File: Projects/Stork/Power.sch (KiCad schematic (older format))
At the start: 14 parts, among them J25 Conn_02x03_Odd_Even, J26 Conn_01x03_Male, J27 Screw_Terminal_01x02, J28 Conn_01x03_Male, J29 Conn_01x03_Male, J30 Conn_01x03_Male, U50 TPS79330-EP, U51 TPS73150DBV

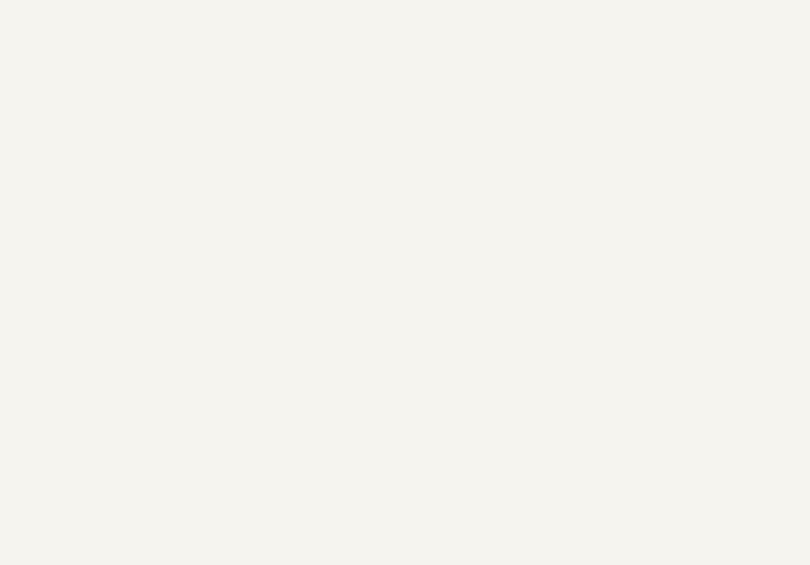
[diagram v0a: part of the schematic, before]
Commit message: added mounting hole in schematic and corresponding footprint on layout
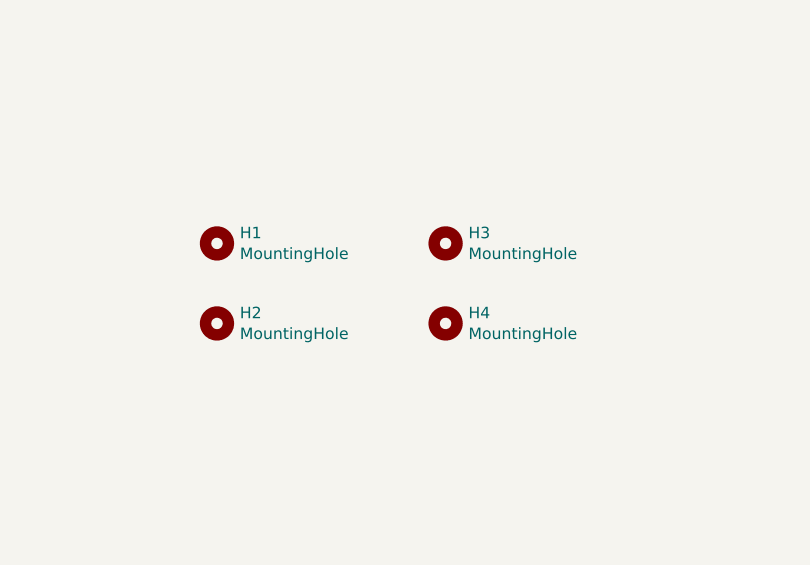
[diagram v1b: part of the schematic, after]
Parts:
- added H1, H2, H3, H4: MountingHole, MountingHole:MountingHole_2.5mm_Pad, symbol Mechanical:MountingHole
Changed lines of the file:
@@
 Wire Wire Line
 	2650 4350 3400 4350
+$Comp
+L Mechanical:MountingHole H1
+U 1 1 5E743F5A
+P 6500 3850
+F 0 "H1" H 6600 3896 50  0000 L CNN
+F 1 "MountingHole" H 6600 3805 50  0000 L CNN
+F 2 "MountingHole:MountingHole_2.5mm_Pad" H 6500 3850 50  0001 C CNN
+F 3 "~" H 6500 3850 50  0001 C CNN
+	1    6500 3850
+	1    0    0    -1
+$EndComp
+$Comp
+L Mechanical:MountingHole H3
+U 1 1 5E74AFC2
+P 7500 3850
+F 0 "H3" H 7600 3896 50  0000 L CNN
+F 1 "MountingHole" H 7600 3805 50  0000 L CNN
+F 2 "MountingHole:MountingHole_2.5mm_Pad" H 7500 3850 50  0001 C CNN
+F 3 "~" H 7500 3850 50  0001 C CNN
+	1    7500 3850
+	1    0    0    -1
+$EndComp
+$Comp
+L Mechanical:MountingHole H2
+U 1 1 5E74C1EE
+P 6500 4200
+F 0 "H2" H 6600 4246 50  0000 L CNN
+F 1 "MountingHole" H 6600 4155 50  0000 L CNN
+F 2 "MountingHole:MountingHole_2.5mm_Pad" H 6500 4200 50  0001 C CNN
+F 3 "~" H 6500 4200 50  0001 C CNN
+	1    6500 4200
+	1    0    0    -1
+$EndComp
+$Comp
+L Mechanical:MountingHole H4
+U 1 1 5E74D363
+P 7500 4200
+F 0 "H4" H 7600 4246 50  0000 L CNN
+F 1 "MountingHole" H 7600 4155 50  0000 L CNN
+F 2 "MountingHole:MountingHole_2.5mm_Pad" H 7500 4200 50  0001 C CNN
+F 3 "~" H 7500 4200 50  0001 C CNN
+	1    7500 4200
+	1    0    0    -1
+$EndComp
 $EndSCHEMATC

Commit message: changed power pin to dc barrel jack
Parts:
- removed J27: Screw_Terminal_01x02, Connector_Molex:Molex_KK-254_AE-6410-02A_1x02_P2.54mm_Vertical, symbol Connector:Screw_Terminal_01x02
- added J?: Barrel_Jack_Switch, footprint:FC681465P, symbol Connector:Barrel_Jack_Switch
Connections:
- wire segments 58 -> 59
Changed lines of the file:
@@
 	1    0    0    -1
 $EndComp
-$Comp
-L Connector:Screw_Terminal_01x02 J27
-U 1 1 5E4E8DF0
-P 1450 2200
-F 0 "J27" H 1530 2192 50  0000 L CNN
-F 1 "Screw_Terminal_01x02" H 1530 2101 50  0000 L CNN
-F 2 "Connector_Molex:Molex_KK-254_AE-6410-02A_1x02_P2.54mm_Vertical" H 1450 2200 50  0001 C CNN
-F 3 "~" H 1450 2200 50  0001 C CNN
-	1    1450 2200
-	-1   0    0    1
-$EndComp
-$Comp
-L power:GND #PWR0152
-U 1 1 5E4ECFCC
-P 2050 2250
-F 0 "#PWR0152" H 2050 2000 50  0001 C CNN
-F 1 "GND" H 2055 2077 50  0000 C CNN
-F 2 "" H 2050 2250 50  0001 C CNN
-F 3 "" H 2050 2250 50  0001 C CNN
-	1    2050 2250
-	1    0    0    -1
-$EndComp
-Wire Wire Line
-	2050 2200 2050 2250
 Text GLabel 5450 1100 2    50   Input ~ 0
 5V_CoraZ7
@@
 Wire Wire Line
 	5300 2400 5150 2400
-Text GLabel 1950 2100 2    50   Input ~ 0
-V_RAW
-Wire Wire Line
-	1600 2100 1650 2100
-Wire Wire Line
-	1650 2100 1950 2100
-Connection ~ 1650 2100
-Wire Wire Line
-	1650 2200 2050 2200
 Wire Wire Line
 	5150 1100 5450 1100
@@
 	1    0    0    -1
 $EndComp
+$Comp
+L Connector:Barrel_Jack_Switch J?
+U 1 1 5EA23779
+P 1050 2200
+F 0 "J?" H 1107 2517 50  0000 C CNN
+F 1 "Barrel_Jack_Switch" H 1107 2426 50  0000 C CNN
+F 2 "footprint:FC681465P" H 1100 2160 50  0001 C CNN
+F 3 "~" H 1100 2160 50  0001 C CNN
+	1    1050 2200
+	1    0    0    -1
+$EndComp
+$Comp
+L power:GND #PWR?
+U 1 1 5EA2418A
+P 1550 2350
+F 0 "#PWR?" H 1550 2100 50  0001 C CNN
+F 1 "GND" H 1555 2177 50  0000 C CNN
+F 2 "" H 1550 2350 50  0001 C CNN
+F 3 "" H 1550 2350 50  0001 C CNN
+	1    1550 2350
+	1    0    0    -1
+$EndComp
+Wire Wire Line
+	1350 2300 1550 2300
+Wire Wire Line
+	1550 2300 1550 2350
+Wire Wire Line
+	1350 2200 1550 2200
+Wire Wire Line
+	1550 2200 1550 2300
+Connection ~ 1550 2300
+Text GLabel 1450 2100 2    50   Input ~ 0
+V_RAW
+Wire Wire Line
+	1350 2100 1450 2100
 $EndSCHEMATC

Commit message: added logo
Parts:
- gave numbers to parts that had none: 1
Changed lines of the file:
@@
 $EndComp
 $Comp
-L Connector:Barrel_Jack_Switch J?
+L Connector:Barrel_Jack_Switch J1
 U 1 1 5EA23779
 P 1050 2200
-F 0 "J?" H 1107 2517 50  0000 C CNN
+F 0 "J1" H 1107 2517 50  0000 C CNN
 F 1 "Barrel_Jack_Switch" H 1107 2426 50  0000 C CNN
 F 2 "footprint:FC681465P" H 1100 2160 50  0001 C CNN
@@
 $EndComp
 $Comp
-L power:GND #PWR?
+L power:GND #PWR0152
 U 1 1 5EA2418A
 P 1550 2350
-F 0 "#PWR?" H 1550 2100 50  0001 C CNN
+F 0 "#PWR0152" H 1550 2100 50  0001 C CNN
 F 1 "GND" H 1555 2177 50  0000 C CNN
 F 2 "" H 1550 2350 50  0001 C CNN
